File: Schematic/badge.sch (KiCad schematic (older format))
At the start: 42 parts, among them J1 Left2, J10 Left1, J11 Penny2, J12 Penny1, J13 Penny0, J14 Power, J15 Right5, J2 Left3, J3 Bottom, J4 Serial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

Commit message: Added charging hardware
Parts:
- removed J10: Left1, Connectors:GS2, symbol Conn_01x02
- removed J2: Left3, Wire_Pads:SolderWirePad_2x_1mmDrill, symbol Conn_01x02
- removed J3: Bottom, symbol Conn_01x09
- added C14, C17: 4.7uF, Capacitors_SMD:C_0805_HandSoldering, symbol badge-rescue:C
- added C15, C19: 0.1uF, Capacitors_SMD:C_0805_HandSoldering, symbol badge-rescue:C
- added C16, C18: 1uF, Capacitors_SMD:C_0805_HandSoldering, symbol badge-rescue:C
- added J10: USB_B_Micro, Connectors_USB:USB_Micro-B_Molex_47346-0001, symbol Connector:USB_B_Micro
- added R2: 2k, Resistors_SMD:R_0805_HandSoldering, symbol badge-rescue:R
- added U2: otter_CH330, Housings_SOIC:SOIC-8-1EP_3.9x4.9mm_Pitch1.27mm, symbol CH330-cache:otter_CH330
- added U3: MCP73831-2-OT, Package_TO_SOT_SMD:SOT-23-5, symbol Battery_Management:MCP73831-2-OT
- added U4: TLV1117-33, TO_SOT_Packages_SMD:SOT-223-3_TabPin2, symbol Regulator_Linear:TLV1117-33
- BT1: symbol Battery_Cell -> badge-rescue:Battery_Cell
- C1, C10, C11, C12, C13, C2, C3, C4, C5, C6, C7, C8, C9: symbol C -> badge-rescue:C
- J1: symbol Conn_01x04 -> badge-rescue:Conn_01x04
- J11, J12, J13, J5, J7, J9: symbol Conn_01x01 -> badge-rescue:Conn_01x01
- J14, J15, J4, J6: symbol Conn_01x02 -> badge-rescue:Conn_01x02
- J8: footprint (none) -> Pin_Headers:Pin_Header_Straight_1x05_Pitch2.54mm; symbol Conn_01x05 -> badge-rescue:Conn_01x05
- LED1, LED10, LED2, LED3, LED4, LED5, LED6, LED7, LED8, LED9: symbol WS2812B -> badge-rescue:WS2812B
- LS1: symbol PKMCS0909E4000-R1 -> badge-rescue:PKMCS0909E4000-R1
- R1: symbol R -> badge-rescue:R
- U1: symbol ESP32-WROOM -> badge-rescue:ESP32-WROOM
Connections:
- net labels added: VBUS, VDDA
- net labels removed: CLK, CMD, IO2, IO26, SD0, SD1, SD2, SD3, VN, VP
- wire segments 78 -> 133
- no-connect marks 3 -> 12
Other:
- note added: "Check if is 3v output later\n"
- moved on the sheet: BT1, J11, J12, J13, J14, J15, J5, LS1

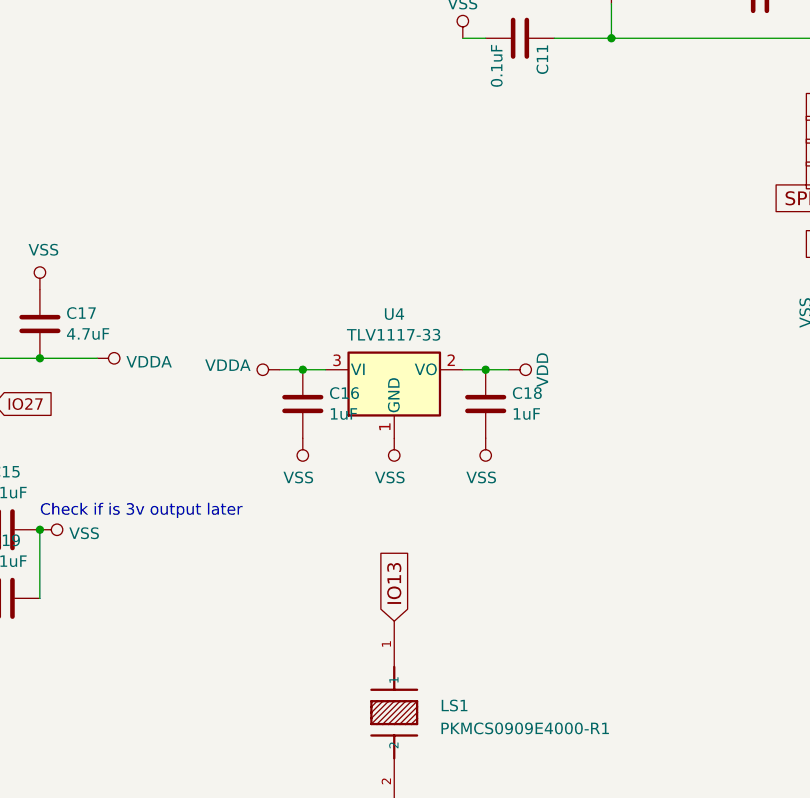
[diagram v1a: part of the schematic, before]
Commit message: Added charging hardware
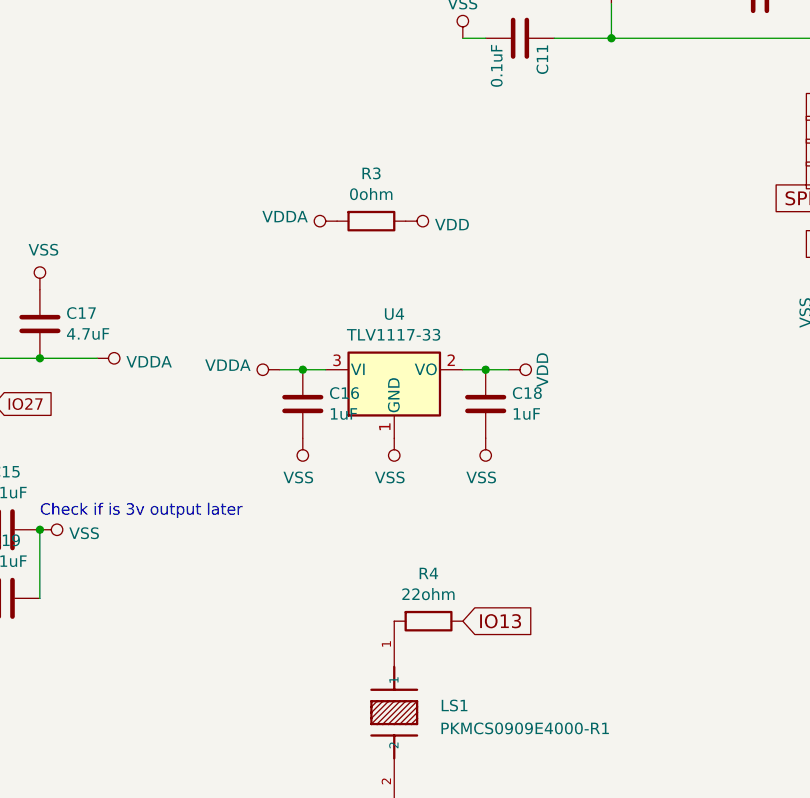
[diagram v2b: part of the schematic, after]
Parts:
- added R3: 0ohm, Resistors_SMD:R_0805_HandSoldering, symbol badge-rescue:R
- added R4: 22ohm, Resistors_SMD:R_0805_HandSoldering, symbol badge-rescue:R
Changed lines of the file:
@@
 	1    0    0    -1
 $EndComp
-Text GLabel 5700 6400 1    60   Input ~ 0
+Text GLabel 6000 6400 2    60   Input ~ 0
 IO13
 $Comp
@@
 NoConn ~ 7800 4050
 NoConn ~ 7800 4650
+$Comp
+L badge-rescue:R R3
+U 1 1 5C3808AE
+P 5600 4650
+F 0 "R3" V 5393 4650 50  0000 C CNN
+F 1 "0ohm" V 5484 4650 50  0000 C CNN
+F 2 "Resistors_SMD:R_0805_HandSoldering" V 5530 4650 50  0001 C CNN
+F 3 "" H 5600 4650 50  0001 C CNN
+	1    5600 4650
+	0    1    1    0
+$EndComp
+$Comp
+L badge-rescue:R R4
+U 1 1 5C3809AF
+P 5850 6400
+F 0 "R4" V 5643 6400 50  0000 C CNN
+F 1 "22ohm" V 5734 6400 50  0000 C CNN
+F 2 "Resistors_SMD:R_0805_HandSoldering" V 5780 6400 50  0001 C CNN
+F 3 "" H 5850 6400 50  0001 C CNN
+	1    5850 6400
+	0    1    1    0
+$EndComp
+$Comp
+L power:VDDA #PWR031
+U 1 1 5C380B3D
+P 5450 4650
+F 0 "#PWR031" H 5450 4500 50  0001 C CNN
+F 1 "VDDA" V 5468 4778 50  0000 L CNN
+F 2 "" H 5450 4650 50  0001 C CNN
+F 3 "" H 5450 4650 50  0001 C CNN
+	1    5450 4650
+	0    -1   -1   0
+$EndComp
+$Comp
+L power:VDD #PWR032
+U 1 1 5C380CD6
+P 5750 4650
+F 0 "#PWR032" H 5750 4500 50  0001 C CNN
+F 1 "VDD" V 5767 4778 50  0000 L CNN
+F 2 "" H 5750 4650 50  0001 C CNN
+F 3 "" H 5750 4650 50  0001 C CNN
+	1    5750 4650
+	0    1    1    0
+$EndComp
 $EndSCHEMATC

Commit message: Ordered V3
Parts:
- removed J15: Right5, Connectors:GS2, symbol badge-rescue:Conn_01x02
- removed J6: Right1, Wire_Pads:SolderWirePad_2x_1mmDrill, symbol badge-rescue:Conn_01x02
- J1: footprint Wire_Pads:SolderWirePad_4xInline_1mmDrill -> Pin_Headers:Pin_Header_Straight_1x04_Pitch2.54mm
- U2: symbol CH330-cache:otter_CH330 -> badge-rescue:otter_CH330-CH330-cache
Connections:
- net labels removed: GND
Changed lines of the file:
@@
 	7050 3500 6950 3500
 Connection ~ 7050 3500
-$Comp
-L power:GND #PWR05
-U 1 1 5AD69A65
-P 6950 3500
-F 0 "#PWR05" H 6950 3250 50  0001 C CNN
-F 1 "GND" H 6950 3350 50  0000 C CNN
-F 2 "" H 6950 3500 50  0001 C CNN
-F 3 "" H 6950 3500 50  0001 C CNN
-	1    6950 3500
-	0    1    1    0
-$EndComp
 Wire Wire Line
 	6400 3850 6650 3850
@@
 F 0 "J1" H 1150 3350 50  0000 C CNN
 F 1 "Left2" H 1150 2850 50  0000 C CNN
-F 2 "Wire_Pads:SolderWirePad_4xInline_1mmDrill" H 1150 3150 50  0001 C CNN
+F 2 "Pin_Headers:Pin_Header_Straight_1x04_Pitch2.54mm" H 1150 3150 50  0001 C CNN
 F 3 "" H 1150 3150 50  0001 C CNN
 	1    1150 3150
-	-1   0    0    1
-$EndComp
-$Comp
-L badge-rescue:Conn_01x02 J6
-U 1 1 5AD7DC83
-P 2900 2650
-F 0 "J6" H 2900 2750 50  0000 C CNN
-F 1 "Right1" H 2900 2450 50  0000 C CNN
-F 2 "Wire_Pads:SolderWirePad_2x_1mmDrill" H 2900 2650 50  0001 C CNN
-F 3 "" H 2900 2650 50  0001 C CNN
-	1    2900 2650
 	-1   0    0    1
 $EndComp
@@
 	-1   0    0    1
 $EndComp
-Text GLabel 3100 2550 2    60   Input ~ 0
-IO23
-Text GLabel 3100 2650 2    60   Input ~ 0
-IO22
 Text GLabel 3100 2950 2    60   Input ~ 0
 IO21
@@
 	0    1    1    0
 $EndComp
-$Comp
-L badge-rescue:Conn_01x02 J15
-U 1 1 5AF92DFF
-P 3700 3050
-F 0 "J15" H 3700 3150 50  0000 C CNN
-F 1 "Right5" H 3700 2850 50  0000 C CNN
-F 2 "Connectors:GS2" H 3700 3050 50  0001 C CNN
-F 3 "" H 3700 3050 50  0001 C CNN
-	1    3700 3050
-	-1   0    0    1
-$EndComp
-Text GLabel 3900 2950 2    60   Input ~ 0
-IO16
-Text GLabel 3900 3050 2    60   Input ~ 0
-IO17
 $Comp
 L badge-rescue:PKMCS0909E4000-R1 LS1
@@
 $EndComp
 $Comp
-L CH330-cache:otter_CH330 U2
+L badge-rescue:otter_CH330-CH330-cache U2
 U 1 1 5C344C72
 P 3250 6150
@@
 	0    1    1    0
 $EndComp
+$Comp
+L power:VSS #PWR0102
+U 1 1 5C39B3AF
+P 6950 3500
+F 0 "#PWR0102" H 6950 3350 50  0001 C CNN
+F 1 "VSS" V 7000 3500 50  0000 L CNN
+F 2 "" H 6950 3500 50  0001 C CNN
+F 3 "" H 6950 3500 50  0001 C CNN
+	1    6950 3500
+	0    -1   -1   0
+$EndComp
 $EndSCHEMATC
